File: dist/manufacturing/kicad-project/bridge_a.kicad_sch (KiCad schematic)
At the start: 14 parts, among them J2 J2, Q6 CSD19534Q5A, Q7 CSD19534Q5A, Q8 CSD19534Q5A, Q9 CSD19534Q5A

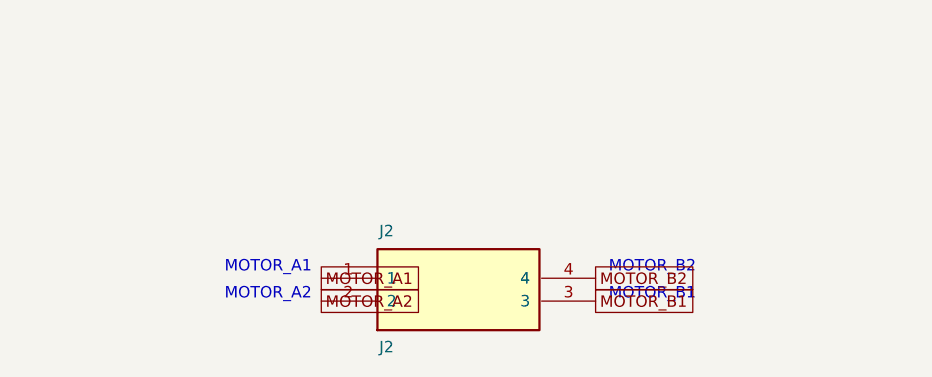
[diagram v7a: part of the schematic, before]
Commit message: Complete top-side routing and verify reference-board ECO
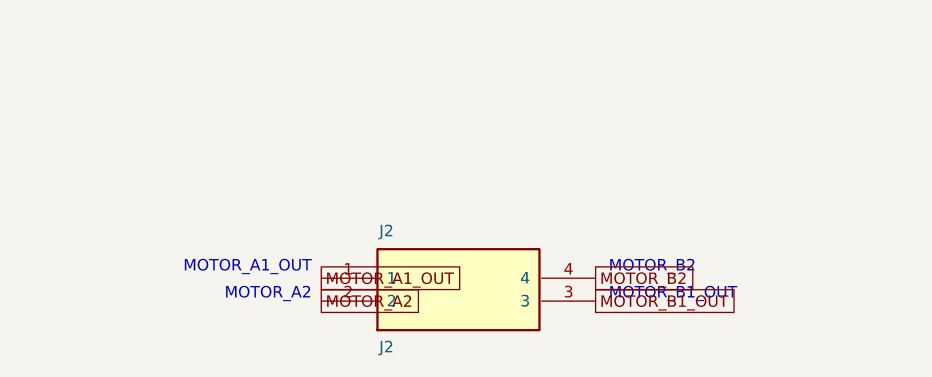
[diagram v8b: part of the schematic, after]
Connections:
- net MOTOR_A1: no longer J2.1
- net MOTOR_B1 renamed MOTOR_B1_OUT
- new net MOTOR_A1_OUT: J2.1
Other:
- note added: "MOTOR_A1_OUT"
- note added: "MOTOR_B1_OUT"
- note removed: "MOTOR_B1"
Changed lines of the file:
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@@
     (instances
       (project ""
-        (path "/4ef2daa1-40fc-426a-abb2-c834ba40a3c9/c38cb720-736d-4a35-af65-5b852b488cbf"
+        (path "/953e0ace-4c89-4879-a4e2-9aa73ffc3208/8d69b5d4-a45d-482e-9c35-257666ee621f"
           (reference "Q6")
           (unit 1)
@@
     (instances
       (project ""
-        (path "/4ef2daa1-40fc-426a-abb2-c834ba40a3c9/c38cb720-736d-4a35-af65-5b852b488cbf"
+        (path "/953e0ace-4c89-4879-a4e2-9aa73ffc3208/8d69b5d4-a45d-482e-9c35-257666ee621f"
           (reference "Q7")
           (unit 1)
@@
     (instances
       (project ""
-        (path "/4ef2daa1-40fc-426a-abb2-c834ba40a3c9/c38cb720-736d-4a35-af65-5b852b488cbf"
+        (path "/953e0ace-4c89-4879-a4e2-9aa73ffc3208/8d69b5d4-a45d-482e-9c35-257666ee621f"
           (reference "R38")
           (unit 1)
@@
     (instances
       (project ""
-        (path "/4ef2daa1-40fc-426a-abb2-c834ba40a3c9/c38cb720-736d-4a35-af65-5b852b488cbf"
+        (path "/953e0ace-4c89-4879-a4e2-9aa73ffc3208/8d69b5d4-a45d-482e-9c35-257666ee621f"
           (reference "R39")
           (unit 1)
@@
     (instances
       (project ""
-        (path "/4ef2daa1-40fc-426a-abb2-c834ba40a3c9/c38cb720-736d-4a35-af65-5b852b488cbf"
+        (path "/953e0ace-4c89-4879-a4e2-9aa73ffc3208/8d69b5d4-a45d-482e-9c35-257666ee621f"
           (reference "R40")
           (unit 1)
@@
     (instances
       (project ""
-        (path "/4ef2daa1-40fc-426a-abb2-c834ba40a3c9/c38cb720-736d-4a35-af65-5b852b488cbf"
+        (path "/953e0ace-4c89-4879-a4e2-9aa73ffc3208/8d69b5d4-a45d-482e-9c35-257666ee621f"
           (reference "R41")
           (unit 1)
@@
     (instances
       (project ""
-        (path "/4ef2daa1-40fc-426a-abb2-c834ba40a3c9/c38cb720-736d-4a35-af65-5b852b488cbf"
+        (path "/953e0ace-4c89-4879-a4e2-9aa73ffc3208/8d69b5d4-a45d-482e-9c35-257666ee621f"
           (reference "Q8")
           (unit 1)
@@
     (instances
       (project ""
-        (path "/4ef2daa1-40fc-426a-abb2-c834ba40a3c9/c38cb720-736d-4a35-af65-5b852b488cbf"
+        (path "/953e0ace-4c89-4879-a4e2-9aa73ffc3208/8d69b5d4-a45d-482e-9c35-257666ee621f"
           (reference "Q9")
           (unit 1)
@@
     (instances
       (project ""
-        (path "/4ef2daa1-40fc-426a-abb2-c834ba40a3c9/c38cb720-736d-4a35-af65-5b852b488cbf"
+        (path "/953e0ace-4c89-4879-a4e2-9aa73ffc3208/8d69b5d4-a45d-482e-9c35-257666ee621f"
           (reference "R42")
           (unit 1)
@@
     (instances
       (project ""
-        (path "/4ef2daa1-40fc-426a-abb2-c834ba40a3c9/c38cb720-736d-4a35-af65-5b852b488cbf"
+        (path "/953e0ace-4c89-4879-a4e2-9aa73ffc3208/8d69b5d4-a45d-482e-9c35-257666ee621f"
           (reference "R43")
           (unit 1)
@@
     (instances
       (project ""
-        (path "/4ef2daa1-40fc-426a-abb2-c834ba40a3c9/c38cb720-736d-4a35-af65-5b852b488cbf"
+        (path "/953e0ace-4c89-4879-a4e2-9aa73ffc3208/8d69b5d4-a45d-482e-9c35-257666ee621f"
           (reference "R44")
           (unit 1)
@@
     (instances
       (project ""
-        (path "/4ef2daa1-40fc-426a-abb2-c834ba40a3c9/c38cb720-736d-4a35-af65-5b852b488cbf"
+        (path "/953e0ace-4c89-4879-a4e2-9aa73ffc3208/8d69b5d4-a45d-482e-9c35-257666ee621f"
           (reference "R45")
           (unit 1)
@@
     (instances
       (project ""
-        (path "/4ef2daa1-40fc-426a-abb2-c834ba40a3c9/c38cb720-736d-4a35-af65-5b852b488cbf"
+        (path "/953e0ace-4c89-4879-a4e2-9aa73ffc3208/8d69b5d4-a45d-482e-9c35-257666ee621f"
           (reference "R109")
           (unit 1)
@@
     (instances
       (project ""
-        (path "/4ef2daa1-40fc-426a-abb2-c834ba40a3c9/c38cb720-736d-4a35-af65-5b852b488cbf"
+        (path "/953e0ace-4c89-4879-a4e2-9aa73ffc3208/8d69b5d4-a45d-482e-9c35-257666ee621f"
           (reference "J2")
           (unit 1)
@@
     )
   )
-  (text "MOTOR_A1"
-    (at 374.85749999999996 331.53749999999997 0)
-    (effects
-      (font
-        (size 1.27 1.27)
-        (color 0 0 0 1)
-      )
-      (justify right)
+  (text "GH_A1"
+    (at 237.6075 85.5375 0)
+    (effects
+      (font
+        (size 1.27 1.27)
+        (color 0 0 0 1)
+      )
     )
   )
@@
     )
   )
-  (text "GH_A1"
-    (at 237.6075 85.5375 0)
-    (effects
-      (font
-        (size 1.27 1.27)
-        (color 0 0 0 1)
-      )
+  (text "SENSE_A"
+    (at 262.9575 327.9375 -90)
+    (effects
+      (font
+        (size 1.27 1.27)
+        (color 0 0 0 1)
+      )
+      (justify left)
     )
   )
@@
     )
   )
-  (text "SENSE_A"
-    (at 262.9575 327.9375 -90)
-    (effects
-      (font
-        (size 1.27 1.27)
-        (color 0 0 0 1)
-      )
-      (justify left)
+  (text "GL_A1"
+    (at 432.60749999999996 85.5375 0)
+    (effects
+      (font
+        (size 1.27 1.27)
+        (color 0 0 0 1)
+      )
     )
   )
@@
     )
   )
-  (text "GL_A1"
-    (at 432.60749999999996 85.5375 0)
-    (effects
-      (font
-        (size 1.27 1.27)
-        (color 0 0 0 1)
-      )
-    )
-  )
   (text "MOTOR_A2"
     (at 149.1075 252.03749999999997 0)
@@
   )
   (text "GH_A2"
+    (at 237.6075 220.5375 0)
+    (effects
+      (font
+        (size 1.27 1.27)
+        (color 0 0 0 1)
+      )
+    )
+  )
+  (text "GH_A2"
     (at 149.1075 261.03749999999997 0)
     (effects
@@
     )
   )
-  (text "GH_A2"
-    (at 237.6075 220.5375 0)
+  (text "GL_A2"
+    (at 432.60749999999996 220.5375 0)
     (effects
       (font
@@
     )
   )
-  (text "GL_A2"
-    (at 432.60749999999996 220.5375 0)
-    (effects
-      (font
-        (size 1.27 1.27)
-        (color 0 0 0 1)
-      )
-    )
-  )
   (text "GH_A1_DRV"
     (at 220.3575 85.5375 0)
@@
     )
   )
-  (text "MOTOR_B1"
-    (at 407.8575 334.53749999999997 0)
+  (text "MOTOR_A1_OUT"
+    (at 374.85749999999996 331.53749999999997 0)
+    (effects
+      (font
+        (size 1.27 1.27)
+        (color 0 0 0 1)
+      )
+      (justify right)
+    )
+  )
+  (text "MOTOR_B1_OUT"
+    (at 407.85749999999996 334.53749999999997 0)
     (effects
       (font
@@
     (fields_autoplaced no)
   )
-  (global_label "MOTOR_A1"
+  (global_label "MOTOR_A1_OUT"
     (shape passive)
     (at 375.92 332.74 0)
@@
     (fields_autoplaced no)
   )
-  (global_label "MOTOR_B1"
+  (global_label "MOTOR_B1_OUT"
     (shape passive)
     (at 406.40000000000003 335.28 0)
